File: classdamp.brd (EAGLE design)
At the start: 88.6 x 40.6 mm, 40 parts, among them Q1 BS170, Q2 BS170

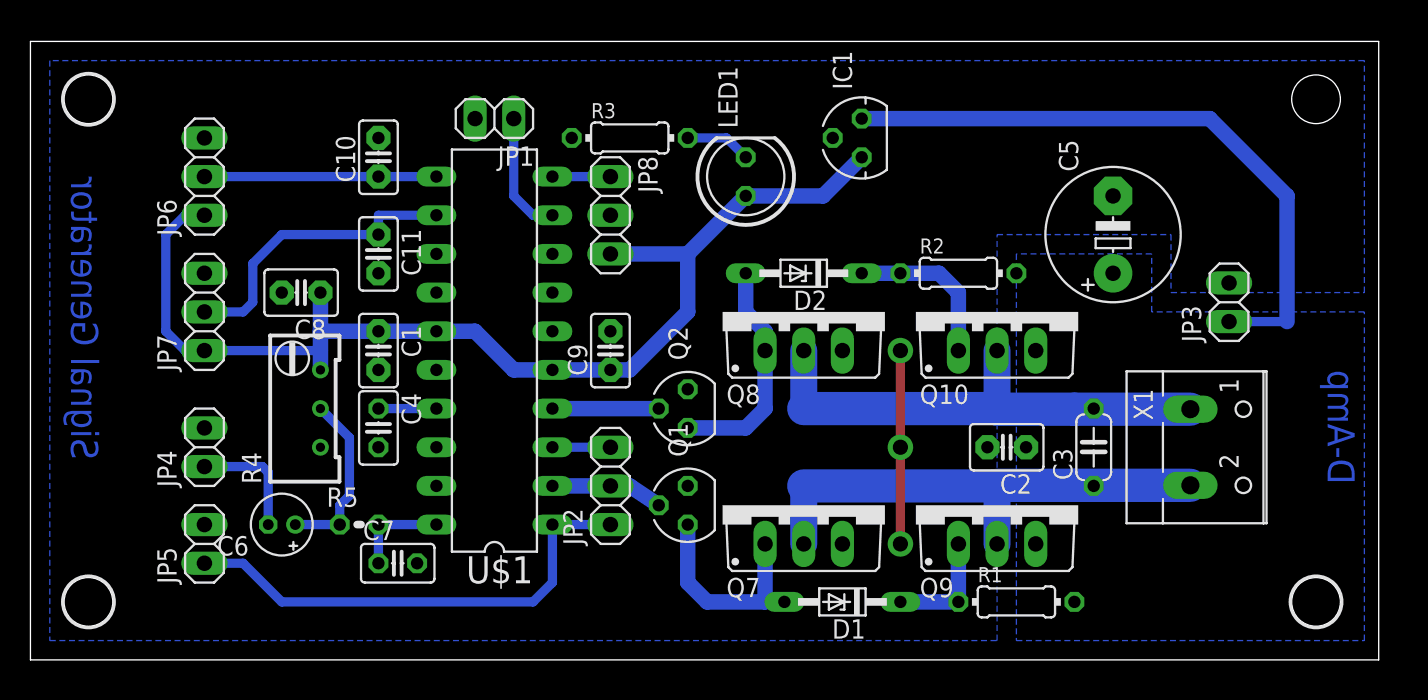
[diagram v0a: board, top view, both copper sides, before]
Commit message: size 37x89 -> 5 pieces on 200x90 PCB
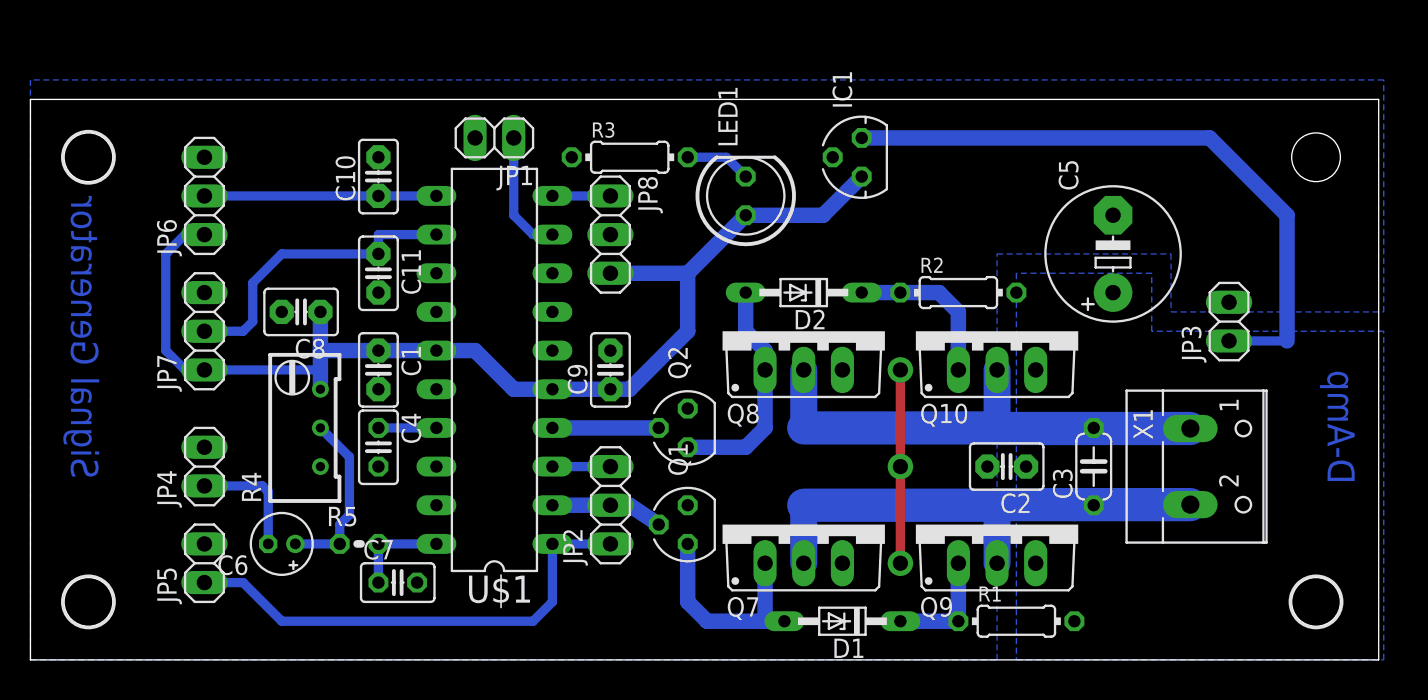
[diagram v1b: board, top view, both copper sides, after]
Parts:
- moved H1 3.81 mm to (3.81, 33.0)
- moved H2 3.81 mm to (84.5, 33.0)
- moved C10 1.27 mm to (22.9, 31.8)
- moved C11 1.27 mm to (22.9, 25.4)
- moved JP1 1.27 mm to (30.5, 34.3)
- moved C2 1.27 mm to (64.1, 12.7)
- moved C3 1.27 mm to (69.8, 12.7)
- moved JP4 1.27 mm to (11.4, 12.7)
- moved Q2 1.27 mm to (43.2, 15.2)
- moved R4 1.27 mm to (17.8, 15.2)
- moved X1 1.27 mm to (77.5, 12.7)
- moved C6 1.27 mm to (16.5, 7.62)
- moved JP5 1.27 mm to (11.4, 6.35)
- moved R5 1.27 mm to (21.6, 7.62)
- moved D1 1.27 mm to (53.3, 2.54)
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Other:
- board size 88.6 x 40.6 mm -> 88.6 x 36.8 mm

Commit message: Changed text size, DRU passed.
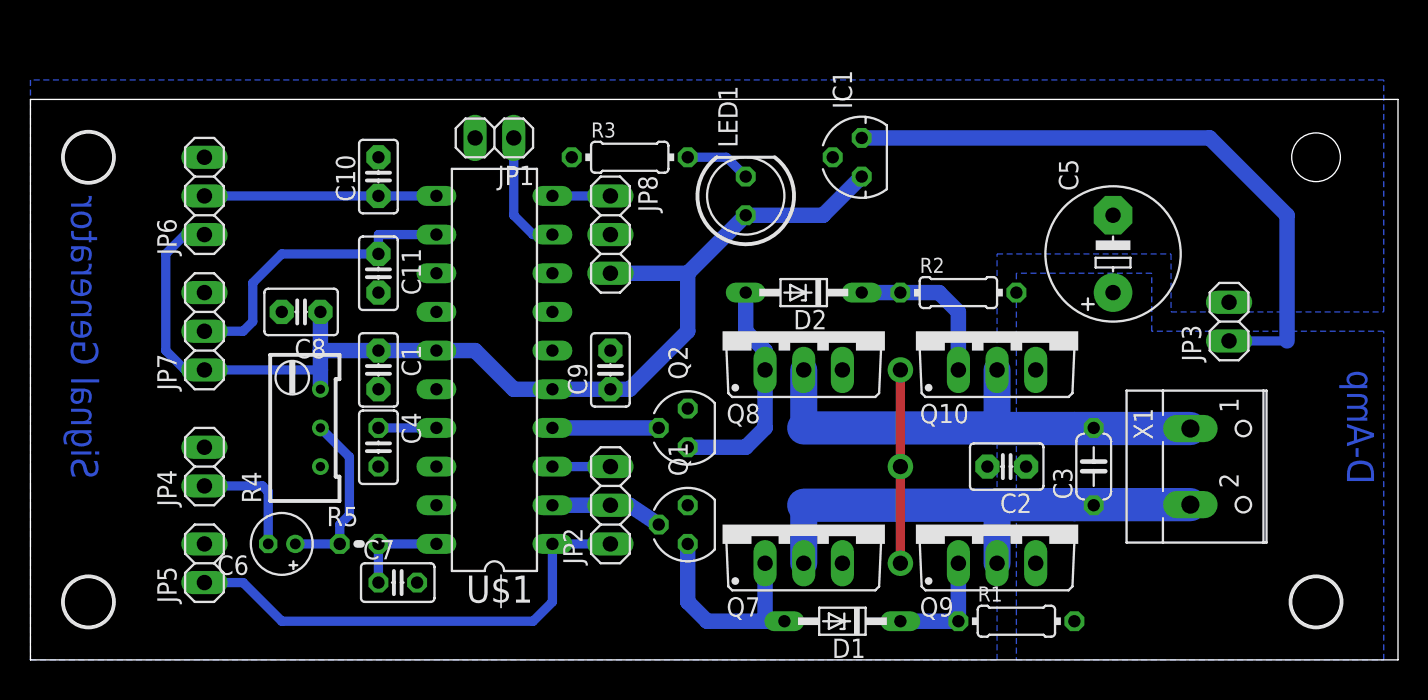
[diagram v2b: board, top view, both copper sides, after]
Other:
- board size 88.6 x 36.8 mm -> 89.8 x 36.8 mm
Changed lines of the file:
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@@
 <board>
 <plain>
-<wire x1="0" y1="0" x2="88.57" y2="0" width="0" layer="20"/>
-<wire x1="88.57" y1="0" x2="88.57" y2="36.82" width="0" layer="20"/>
-<wire x1="88.57" y1="36.82" x2="0" y2="36.82" width="0" layer="20"/>
+<wire x1="0" y1="0" x2="89.84" y2="0" width="0" layer="20"/>
+<wire x1="89.84" y1="0" x2="89.84" y2="36.82" width="0" layer="20"/>
+<wire x1="89.84" y1="36.82" x2="0" y2="36.82" width="0" layer="20"/>
 <wire x1="0" y1="36.82" x2="0" y2="0" width="0" layer="20"/>
-<text x="86.995" y="19.05" size="1.778" layer="16" font="vector" rot="MR270">D-Amp</text>
-<text x="4.445" y="30.48" size="1.778" layer="16" font="vector" rot="MR270">Signal Generator</text>
+<text x="88.265" y="19.05" size="1.778" layer="16" font="vector" ratio="14" rot="MR270">D-Amp</text>
+<text x="4.445" y="30.48" size="1.778" layer="16" font="vector" ratio="15" rot="MR270">Signal Generator</text>
 </plain>
 <attributes>

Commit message: Just few small things...
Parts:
- removed C3: 47n, resistor:C050-024X044
- added C12: 47n, capacitor-wima:C5B3.5
- C4: value 47n -> 100n; device resistor:C025-025X050 -> capacitor-wima:C2.5-2
- C7: value 1nF -> 1n; device resistor:C025-025X050 -> capacitor-wima:C2.5-2
- C8: device capacitor-wima:C2.5-3 -> capacitor-wima:C2.5-2
- moved C2 2.54 mm to (61.6, 12.7)
- turned JP1 to 0 degrees
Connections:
- net N$11: now also C12.1; no longer C3.1
- net N$13: now also C12.2; no longer C3.2
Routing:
- net N$13: track 34.3 -> 33.1 mm
- net N$11: track 34.3 -> 33.1 mm
- net ONOFF: track 8.15 -> 9.20 mm
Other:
- board size 89.8 x 36.8 mm -> 88.6 x 36.8 mm
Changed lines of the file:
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@@
 <board>
 <plain>
-<wire x1="0" y1="0" x2="89.84" y2="0" width="0" layer="20"/>
-<wire x1="89.84" y1="0" x2="89.84" y2="36.82" width="0" layer="20"/>
-<wire x1="89.84" y1="36.82" x2="0" y2="36.82" width="0" layer="20"/>
+<wire x1="0" y1="0" x2="88.57" y2="0" width="0" layer="20"/>
+<wire x1="88.57" y1="0" x2="88.57" y2="36.82" width="0" layer="20"/>
+<wire x1="88.57" y1="36.82" x2="0" y2="36.82" width="0" layer="20"/>
 <wire x1="0" y1="36.82" x2="0" y2="0" width="0" layer="20"/>
-<text x="88.265" y="19.05" size="1.778" layer="16" font="vector" ratio="14" rot="MR270">D-Amp</text>
+<text x="86.995" y="19.05" size="1.778" layer="16" font="vector" ratio="14" rot="MR270">D-Amp</text>
 <text x="4.445" y="30.48" size="1.778" layer="16" font="vector" ratio="15" rot="MR270">Signal Generator</text>
 </plain>
@@
 <element name="IC1" library="v-reg" package="78LXX" value="" x="54.61" y="33.02" rot="R90"/>
 <element name="C1" library="capacitor-wima" package="C2.5-2" value="100n" x="22.86" y="19.05" rot="R270"/>
-<element name="C2" library="capacitor-wima" package="C2.5-3" value="100n" x="64.135" y="12.7" rot="R180"/>
+<element name="C2" library="capacitor-wima" package="C2.5-3" value="100n" x="61.595" y="12.7" rot="R180"/>
 <element name="D1" library="diode" package="DO34Z7" value="6.3V" x="53.34" y="2.54" rot="R180"/>
 <element name="Q1" library="transistor-small-signal" package="SOT54E" value="BS170" x="43.18" y="8.89" rot="R90"/>
@@
 <element name="D2" library="diode" package="DO34Z7" value="6.3V" x="50.8" y="24.13" rot="R180"/>
 <element name="Q2" library="transistor-small-signal" package="SOT54E" value="BS170" x="43.18" y="15.24" rot="R90"/>
-<element name="C3" library="resistor" package="C050-024X044" value="47n" x="69.85" y="12.7" rot="R90"/>
 <element name="R2" library="resistor" package="0204/7" value="1k" x="60.96" y="24.13"/>
-<element name="C4" library="resistor" package="C025-025X050" value="47n" x="22.86" y="13.97" rot="R270"/>
 <element name="JP3" library="pinhead" package="1X02" value="" x="78.74" y="22.225" rot="R90"/>
 <element name="JP4" library="pinhead" package="1X02" value="Audio_In" x="11.43" y="12.7" rot="R90"/>
@@
 <element name="C6" library="resistor" package="E1,8-4" value="10uF" x="16.51" y="7.62" rot="R180"/>
 <element name="R5" library="resistor" package="0204V" value="10k" x="21.59" y="7.62"/>
-<element name="C7" library="resistor" package="C025-025X050" value="1nF" x="24.13" y="5.08"/>
 <element name="U$1" library="avr-7" package="DIL20" value="TINY26P" x="30.48" y="19.05" rot="R90"/>
-<element name="C8" library="capacitor-wima" package="C2.5-3" value="100n" x="17.78" y="22.86" rot="R180"/>
+<element name="C8" library="capacitor-wima" package="C2.5-2" value="100n" x="17.78" y="22.86" rot="R180"/>
 <element name="C9" library="capacitor-wima" package="C2.5-2" value="100n" x="38.1" y="19.05" rot="R90"/>
 <element name="C10" library="capacitor-wima" package="C2.5-2" value="100n" x="22.86" y="31.75" rot="R90"/>
@@
 <element name="JP2" library="pinhead" package="1X03" value="ISP1" x="38.1" y="10.16" rot="R90"/>
 <element name="JP8" library="pinhead" package="1X03" value="ISP2" x="38.1" y="27.94" rot="R270"/>
-<element name="JP1" library="pinhead" package="1X02" value="On/Off" x="30.48" y="34.29" rot="R180"/>
+<element name="JP1" library="pinhead" package="1X02" value="On/Off" x="30.48" y="34.29"/>
+<element name="C4" library="capacitor-wima" package="C2.5-2" value="100n" x="22.86" y="13.97" rot="R270"/>
+<element name="C7" library="capacitor-wima" package="C2.5-2" value="1n" x="24.13" y="5.08"/>
+<element name="C12" library="capacitor-wima" package="C5B3.5" value="47n" x="69.85" y="12.7" rot="R90"/>
 </elements>
 <signals>
@@
 <polygon width="0.254" layer="16" isolate="0.4064">
 <vertex x="64.77" y="25.4"/>
+<vertex x="64.77" y="13.97"/>
+<vertex x="62.23" y="13.97"/>
+<vertex x="62.23" y="11.43"/>
+<vertex x="64.77" y="11.43"/>
 <vertex x="64.77" y="0"/>
 <vertex x="88.9" y="0"/>
@@
 <contactref element="JP4" pad="2"/>
 <contactref element="JP6" pad="3"/>
-<contactref element="C7" pad="2"/>
 <contactref element="JP7" pad="3"/>
 <contactref element="U$1" pad="16"/>
@@
 <contactref element="Q7" pad="S"/>
 <contactref element="Q8" pad="S"/>
-<contactref element="C4" pad="2"/>
 <contactref element="JP5" pad="2"/>
 <via x="57.15" y="19.05" extent="1-16" drill="1" diameter="1.6764" shape="square"/>
@@
 <vertex x="0" y="0"/>
 <vertex x="63.5" y="0"/>
+<vertex x="63.5" y="11.43"/>
+<vertex x="60.96" y="11.43"/>
+<vertex x="60.96" y="13.97"/>
+<vertex x="63.5" y="13.97"/>
 <vertex x="63.5" y="26.67"/>
 <vertex x="74.93" y="26.67"/>
@@
 <contactref element="JP8" pad="2"/>
 <via x="57.15" y="12.7" extent="1-16" drill="1" diameter="1.6764" shape="square"/>
+<contactref element="C4" pad="2"/>
+<contactref element="C7" pad="2"/>
 </signal>
 <signal name="N$11">
 <contactref element="Q9" pad="D"/>
 <contactref element="Q7" pad="D"/>
-<contactref element="C3" pad="1"/>
 <contactref element="X1" pad="2"/>
-<wire x1="76.2" y1="10.2" x2="68.58" y2="10.2" width="2.1844" layer="16"/>
-<wire x1="68.58" y1="10.2" x2="63.5" y2="10.2" width="2.1844" layer="16"/>
+<wire x1="76.2" y1="10.2" x2="69.85" y2="10.2" width="2.1844" layer="16"/>
+<wire x1="69.85" y1="10.2" x2="63.5" y2="10.2" width="2.1844" layer="16"/>
 <wire x1="63.5" y1="10.2" x2="63.5" y2="10.16" width="1.27" layer="16"/>
 <wire x1="63.5" y1="6.35" x2="63.5" y2="10.16" width="1.778" layer="16"/>
-<wire x1="63.5" y1="10.16" x2="50.8" y2="10.16" width="2.1844" layer="16"/>
+<wire x1="63.5" y1="10.16" x2="51.435" y2="10.16" width="2.1844" layer="16"/>
+<wire x1="51.435" y1="10.16" x2="50.8" y2="10.16" width="1.778" layer="16"/>
 <wire x1="50.8" y1="10.16" x2="50.8" y2="6.35" width="1.778" layer="16"/>
-<wire x1="69.85" y1="10.16" x2="68.58" y2="10.2" width="1.27" layer="16"/>
+<contactref element="C12" pad="1"/>
+<wire x1="69.85" y1="10.16" x2="69.85" y2="10.2" width="1.778" layer="16"/>
 </signal>
 <signal name="N$5">
@@
 </signal>
 <signal name="N$13">
-<contactref element="C3" pad="2"/>
 <contactref element="Q10" pad="D"/>
 <contactref element="Q8" pad="D"/>
 <contactref element="X1" pad="1"/>
-<wire x1="76.2" y1="15.2" x2="68.58" y2="15.2" width="2.1844" layer="16"/>
-<wire x1="68.58" y1="15.2" x2="63.5" y2="15.2" width="2.1844" layer="16"/>
+<wire x1="76.2" y1="15.2" x2="69.85" y2="15.2" width="2.1844" layer="16"/>
+<wire x1="69.85" y1="15.2" x2="63.5" y2="15.2" width="2.1844" layer="16"/>
 <wire x1="63.5" y1="15.2" x2="63.5" y2="15.24" width="1.27" layer="16"/>
 <wire x1="63.5" y1="19.05" x2="63.5" y2="15.24" width="1.778" layer="16"/>
-<wire x1="63.5" y1="15.24" x2="50.8" y2="15.24" width="2.1844" layer="16"/>
+<wire x1="63.5" y1="15.24" x2="51.435" y2="15.24" width="2.1844" layer="16"/>
+<wire x1="51.435" y1="15.24" x2="50.8" y2="15.24" width="1.778" layer="16"/>
 <wire x1="50.8" y1="15.24" x2="50.8" y2="19.05" width="1.778" layer="16"/>
-<wire x1="69.85" y1="15.24" x2="68.58" y2="15.2" width="1.27" layer="16"/>
+<contactref element="C12" pad="2"/>
+<wire x1="69.85" y1="15.24" x2="69.85" y2="15.2" width="1.778" layer="16"/>
 </signal>
 <signal name="OUT1">
@@
 <signal name="ADC1">
 <contactref element="R5" pad="2"/>
-<contactref element="C7" pad="1"/>
 <contactref element="U$1" pad="20"/>
 <wire x1="26.67" y1="7.62" x2="22.86" y2="7.62" width="0.6096" layer="16"/>
+<contactref element="C7" pad="1"/>
 <wire x1="22.86" y1="7.62" x2="22.86" y2="5.08" width="0.6096" layer="16"/>
 </signal>
@@
 <contactref element="U$1" pad="17"/>
 <contactref element="C4" pad="1"/>
-<wire x1="22.86" y1="15.24" x2="26.67" y2="15.24" width="0.6096" layer="16"/>
+<wire x1="26.67" y1="15.24" x2="22.86" y2="15.24" width="0.6096" layer="16"/>
 </signal>
 <signal name="OUT2">
@@
 <contactref element="U$1" pad="9"/>
 <wire x1="34.29" y1="27.94" x2="33.02" y2="27.94" width="0.6096" layer="16"/>
-<wire x1="33.02" y1="27.94" x2="31.75" y2="29.21" width="0.6096" layer="16"/>
-<wire x1="31.75" y1="29.21" x2="31.75" y2="34.29" width="0.6096" layer="16"/>
+<wire x1="33.02" y1="27.94" x2="29.21" y2="31.75" width="0.6096" layer="16"/>
+<wire x1="29.21" y1="31.75" x2="29.21" y2="34.29" width="0.6096" layer="16"/>
 </signal>
 </signals>
